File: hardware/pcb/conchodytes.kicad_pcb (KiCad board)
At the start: 4 copper layers, 39 x 81.5 mm, 62 parts, among them J1 Conn_02x03_Odd_Even, J10 Battery, J48 USB_C_Receptacle_USB2.0_16P, Q2 AO3407, Q4 FS8205, SW1 Left click, SW2 Right Click, SW3 Middle click, SW54 SW_SPDT, U100 LDO 1V8, U18 TP4056-42-ESOP8, U2 PMW3360, U20 HT7833, U23 DW01A, U54 USBLC6-2SC6, U6 ESP32-S3-WROOM-1, U8 NRF24L01_Breakout

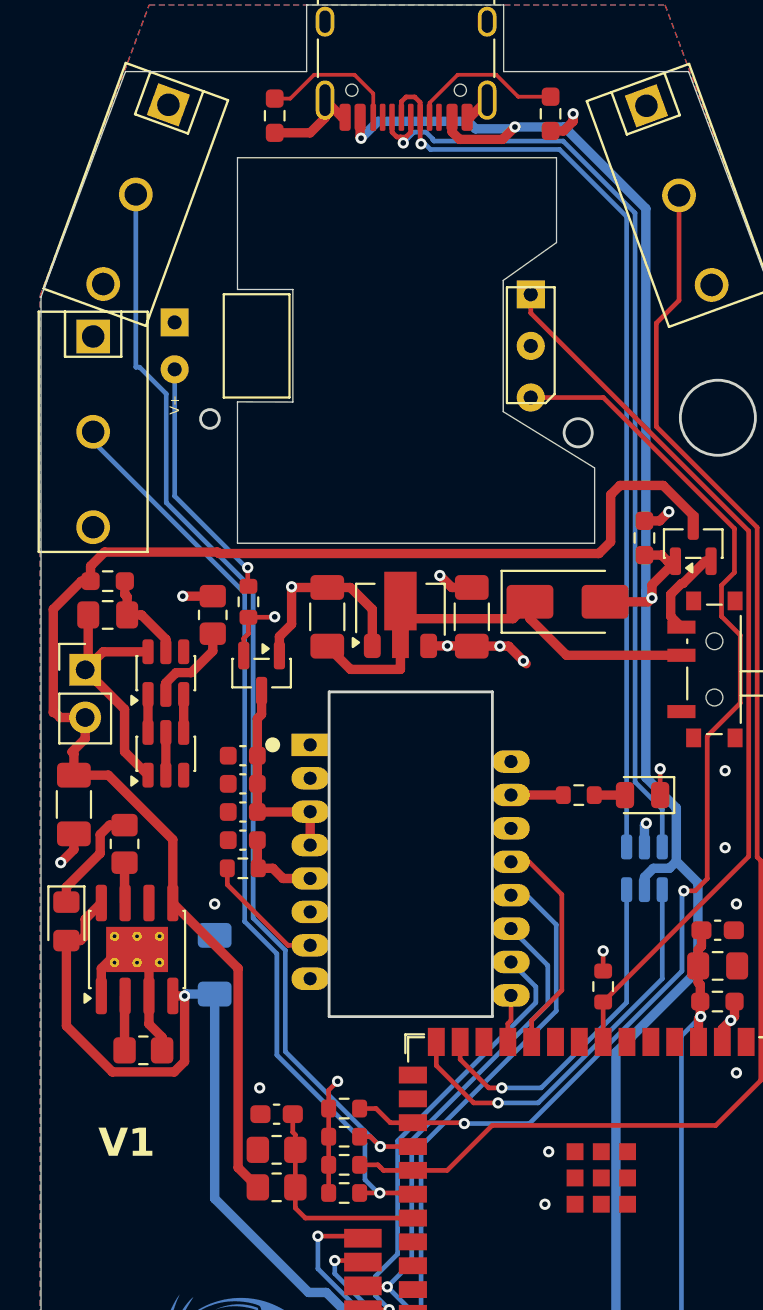
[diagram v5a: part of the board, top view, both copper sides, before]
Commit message: sérigraphie, logos annotés, prêt pour la pré-release
Mae a posé « Conchodytes » et « V1.0.0 08/2026 By mornepousse » au dos, plus le
logo Niphargus en cuivre et le symbole Open Source Hardware.

Les deux logos portaient la référence REF** : annotés HS1 et HS2, sinon le
prochain F8 les traiterait comme des composants fantômes.

Baseline re-référencée sur cet état (DRC 26/20, ERC 14/14) : la sérigraphie
ajoute 1 warning text_thickness, assumé.

Co-Authored-By: Claude Opus 5 <noreply@anthropic.com>
Claude-Session: https://claude.ai/code/session_01GfX5RmekmQi78Dm37qsT4Z
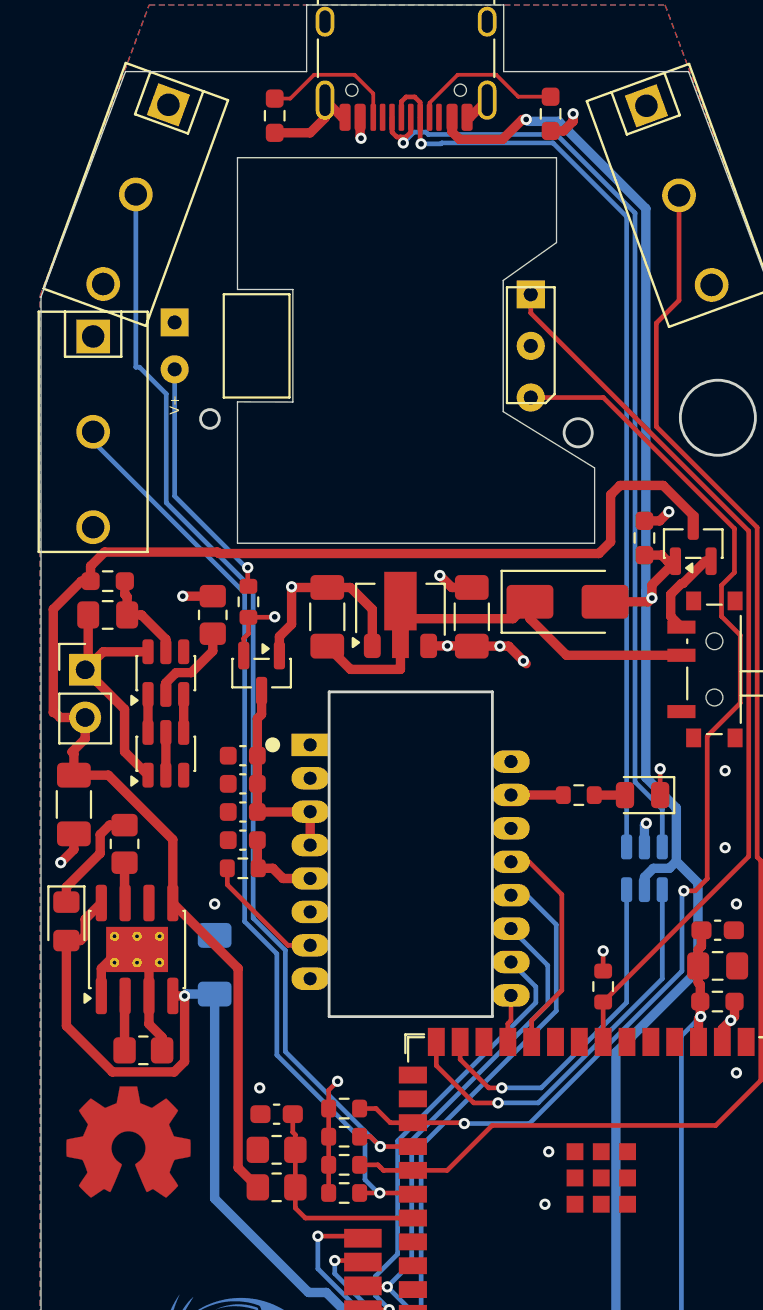
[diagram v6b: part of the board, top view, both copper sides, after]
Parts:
- added HS2: OSHW-Symbol_6.7x6mm_Copper, Symbol:OSHW-Symbol_6.7x6mm_Copper, F.Cu at (81.5, 131.9)
- renumbered REF** to HS1
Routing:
- net +5V: track 166.5 -> 167.7 mm
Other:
- board text added: "V1.0.0 08/2026 By mornepousse"
- board text removed: "V1"

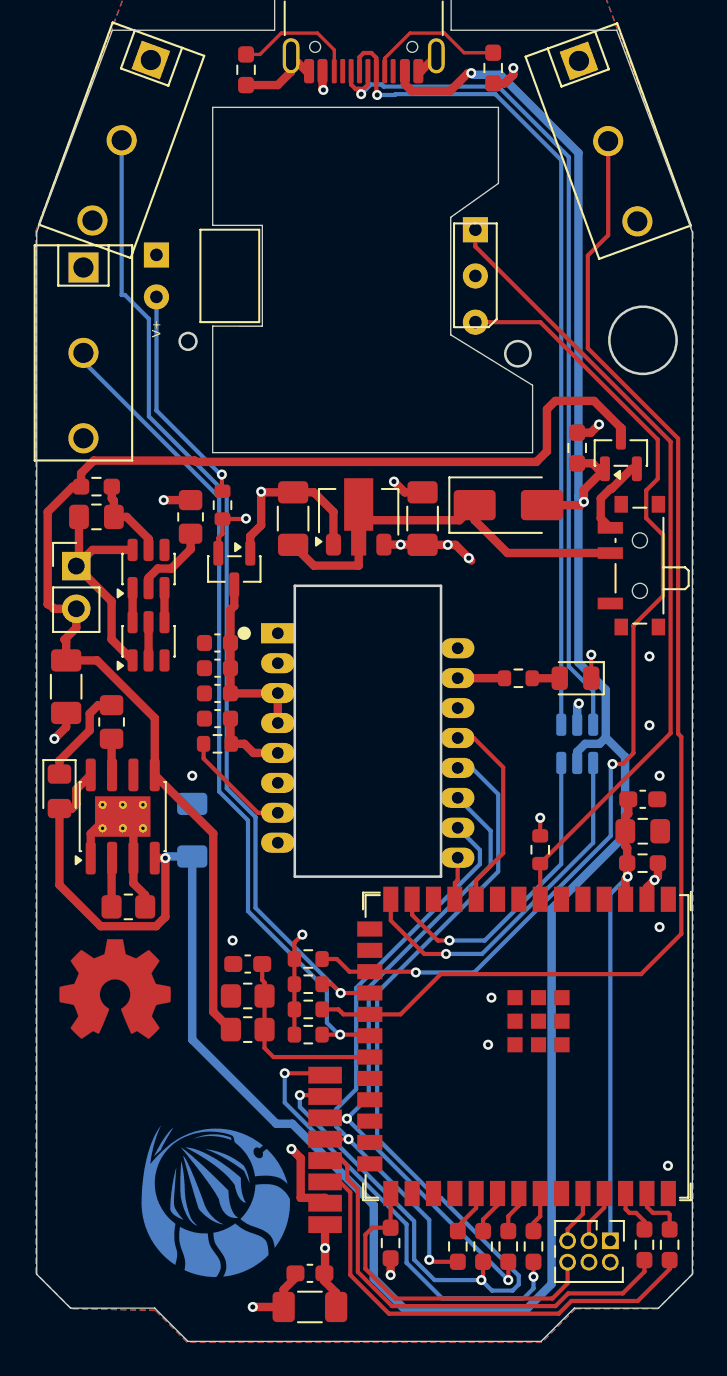
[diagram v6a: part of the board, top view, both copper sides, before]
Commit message: contacts NC des trois clics : anti-rebond par SPDT
Les switches de la coque M100 sont des SPDT. Le schema n'exploitait que COM et
NO, les pins NC portaient un no_connect et leurs pads restaient en l'air.

On lit maintenant les DEUX contacts. Au repos NC est ferme sur COM donc bas et
NO ouvert donc haut ; au clic ils s'inversent. Pendant le rebond les deux sont
hauts : le firmware garde alors l'etat precedent, ce qui supprime le double-clic
sans aucun filtrage temporel.

  SW_LEFT_NC  -> GPIO4    SW_RIGHT_NC -> GPIO5    SW_MID_NC -> GPIO6
  pull-ups 10 k R108/R109/R110, en miroir des R105-R107 des NO

L'ERC y GAGNE 3 erreurs (14 -> 11) : GPIO4/5/6 etaient des pins libres
signalees pin_not_connected. Netlist verifiee, chaque net NC a exactement
3 noeuds. DRC 26/20 inchange, 0 pad non connecte. Placement et routage par Mae.

CORRECTION DE DOCUMENTATION : le README donnait "SW_LEFT 18, SW_RIGHT 19,
SW_MID 20" — ce sont les NUMEROS DE BROCHE du module, pas les GPIO, qui valent
10/11/12. Idem SNS_NCS (GPIO17, broche 10) et SNS_MOTION (GPIO18, broche 11).
Verifie en recoupant lib_symbols, les fils et la netlist. Le tableau donne
desormais les deux colonnes. Le module au BOM est un N8R2 (C2913204), pas le
N16R8 dont parlait le README — la mention de PSRAM octale est retiree.

Co-Authored-By: Claude Opus 5 <noreply@anthropic.com>
Claude-Session: https://claude.ai/code/session_01GfX5RmekmQi78Dm37qsT4Z
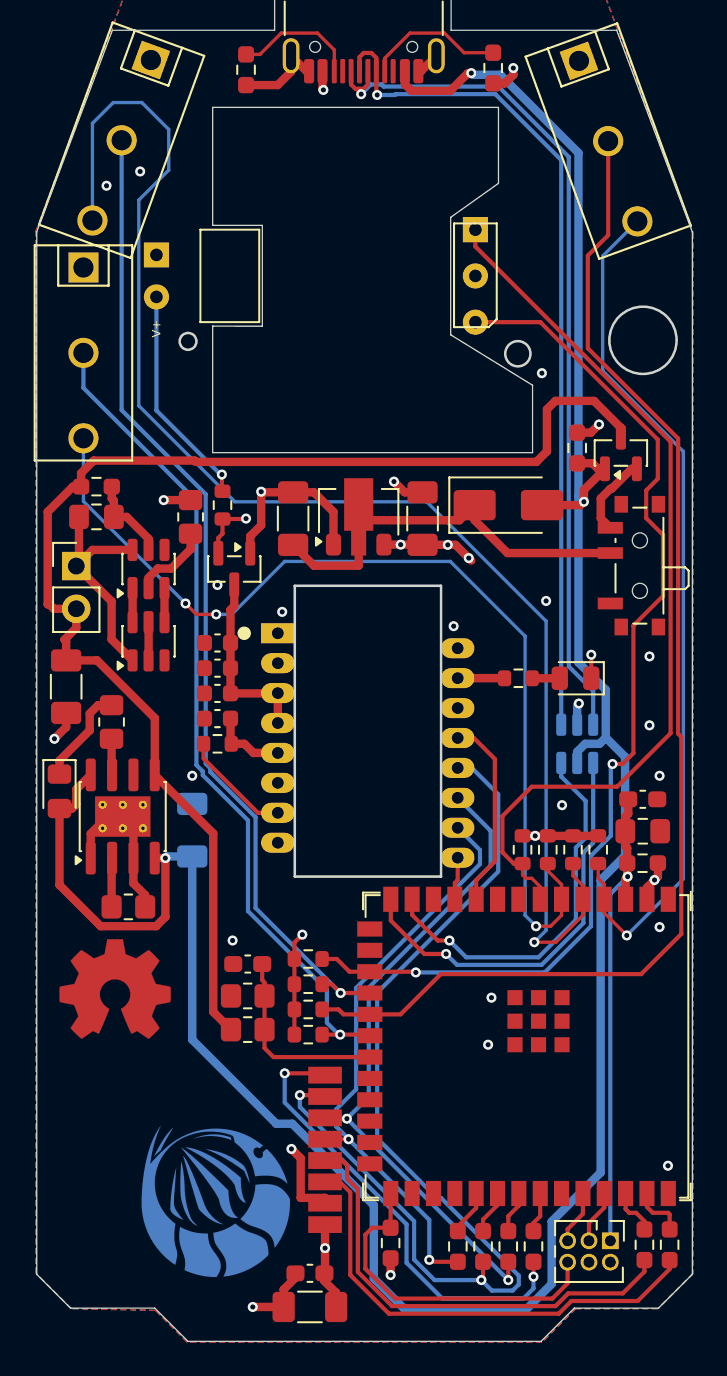
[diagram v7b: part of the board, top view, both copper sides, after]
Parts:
- added R108: 10k, Resistor_SMD:R_0603_1608Metric, F.Cu at (108.8, 123.6)
- added R109: 10k, Resistor_SMD:R_0603_1608Metric, F.Cu at (110.2, 123.6)
- added R110: 10k, Resistor_SMD:R_0603_1608Metric, F.Cu at (107.2, 123.6)
- moved R103 1.05 mm to (105.8, 123.6)
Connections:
- SW1 pad 3: unconnected-(SW1-NC-Pad3) -> SW_LEFT_NC
- SW2 pad 3: unconnected-(SW2-NC-Pad3) -> SW_RIGHT_NC
- SW3 pad 3: unconnected-(SW3-NC-Pad3) -> SW_MID_NC
- U6 pad 4: unconnected-(U6-GPIO4/TOUCH4/ADC1_CH3-Pad4) -> SW_RIGHT_NC
- U6 pad 5: unconnected-(U6-GPIO5/TOUCH5/ADC1_CH4-Pad5) -> SW_LEFT_NC
- U6 pad 6: unconnected-(U6-GPIO6/TOUCH6/ADC1_CH5-Pad6) -> SW_MID_NC
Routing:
- net SW_LEFT_NC: track 0.00 -> 84.5 mm, vias 0 -> 1
- net SW_MID_NC: track 0.00 -> 58.9 mm, vias 0 -> 3
- net SW_RIGHT_NC: track 0.00 -> 51.7 mm, vias 0 -> 1
- net ENC_A: track 47.9 -> 53.2 mm
- net D-_s3: track 18.3 -> 22.8 mm
- net +3.3V: track 31.1 -> 34.5 mm
- net D+_s3: track 21.6 -> 24.6 mm
- net ENC_B: track 60.5 -> 63.0 mm
- net GND: vias 18 -> 26

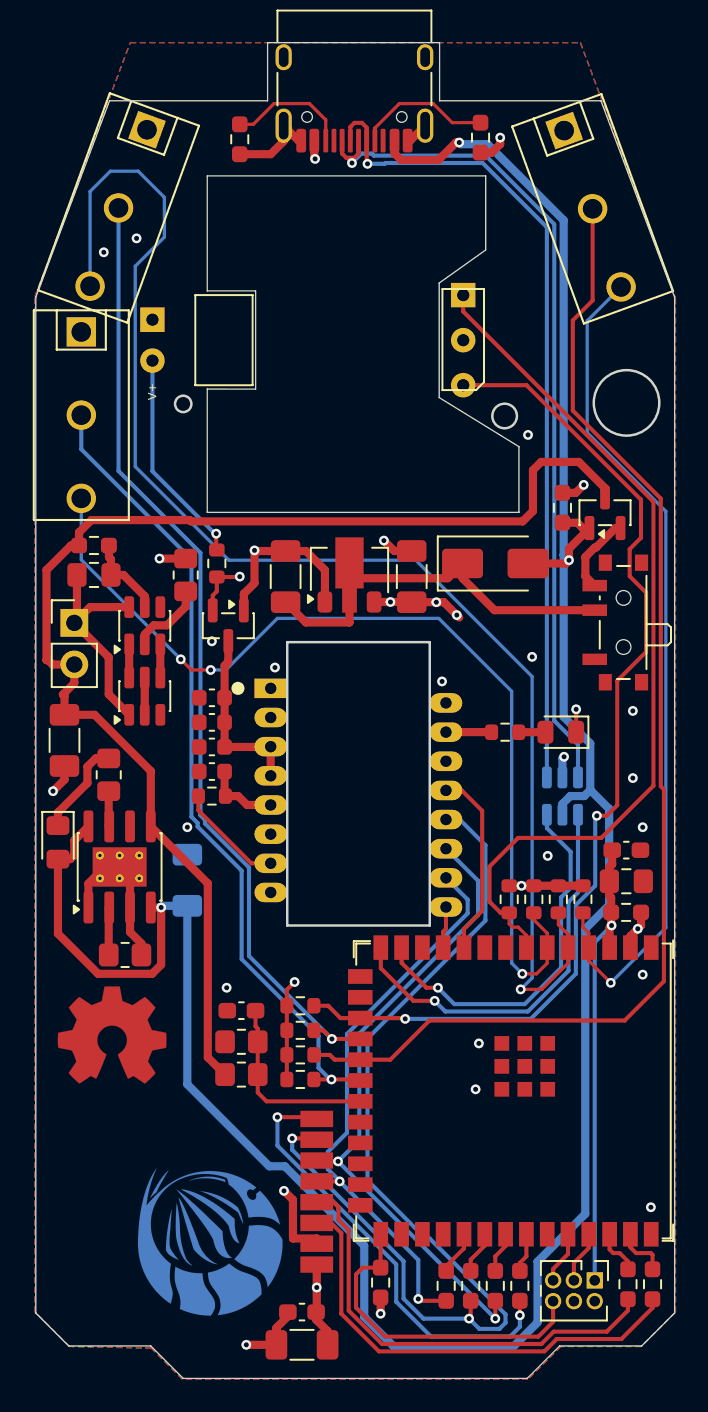
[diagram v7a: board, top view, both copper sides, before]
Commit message: schema REV2 : LQ1 recable, D100 supprimee, VBAT_SENSE sur ADC1, U100 corrige
LQ1 etait cable a l'envers depuis le portage du fork USB-Mouse. Le symbole
Optical_Mouse:LQ ne nommait ses broches que "1, 2, 3", sans fonction, et le
portage a suppose un double phototransistor A/COM/B. Le schema d'origine de la
M100 dit autre chose : broche 1 = DATA, 2 = VCC, 3 = GND.

La carte alimentait donc le capteur a l'envers — son VCC a la masse, sa masse
tiree au 3,3 V par R104. Le courant passait par la diode de substrat interne et
clampait les deux nets a 0,65 V, insensible a la lumiere comme au pilotage.
Deux LQ1 ont ete dessoudes avant que la confrontation au schema source ne donne
la reponse.

  - LQ1.2 -> +3V3, LQ1.3 -> GND, LQ1.1 (DATA) reste sur ENC_A / GPIO7
  - LD1 cathode -> R102 -> GPIO9, renomme ENC_LED : la LED de molette devient
    pilotable, comme sur la M100 d'origine. Gain d'autonomie, et un diagnostic
    qui aurait pris une minute au lieu d'une journee.
  - R102 = 820 ohms : 2,6 mA, le point de fonctionnement d'origine transpose
    du 5 V USB au 3,3 V
  - R104 = 0 ohm (pont vers la masse), R103 conservee
  - symbole LQ : broches nommees DATA / VCC / GND, dans le cache et dans
    optical_mouse.lib, pour que l'erreur soit impossible a refaire

D100 supprimee : le PMW3389 embarque sa LED IR (broche 15 LED_P = anode). La
LED externe etait de surcroit montee a l'envers et bloquait le courant, rendant
le capteur aveugle. R101 = 16 ohms alimentee depuis le rail capteur, renomme
+1V8 -> +2V0.

VBAT_SENSE passe de U6.21 (GPIO13, ADC2_CH2) a U6.12 (GPIO8, ADC1_CH7) :
l'ADC2 de l'ESP32-S3 est partage avec le driver WiFi.

U100 : les numeros de pad du symbole sont corriges — VI porte le pad 3 et VO le
pad 2, soit le brochage reel du XC6206 en SOT-23. Le schema cesse de mentir et
la netlist devient juste d'elle-meme.

Co-Authored-By: Claude Opus 5 (1M context) <noreply@anthropic.com>
Claude-Session: https://claude.ai/code/session_01VhxWZJVUd4SHAcp3eUFVJV
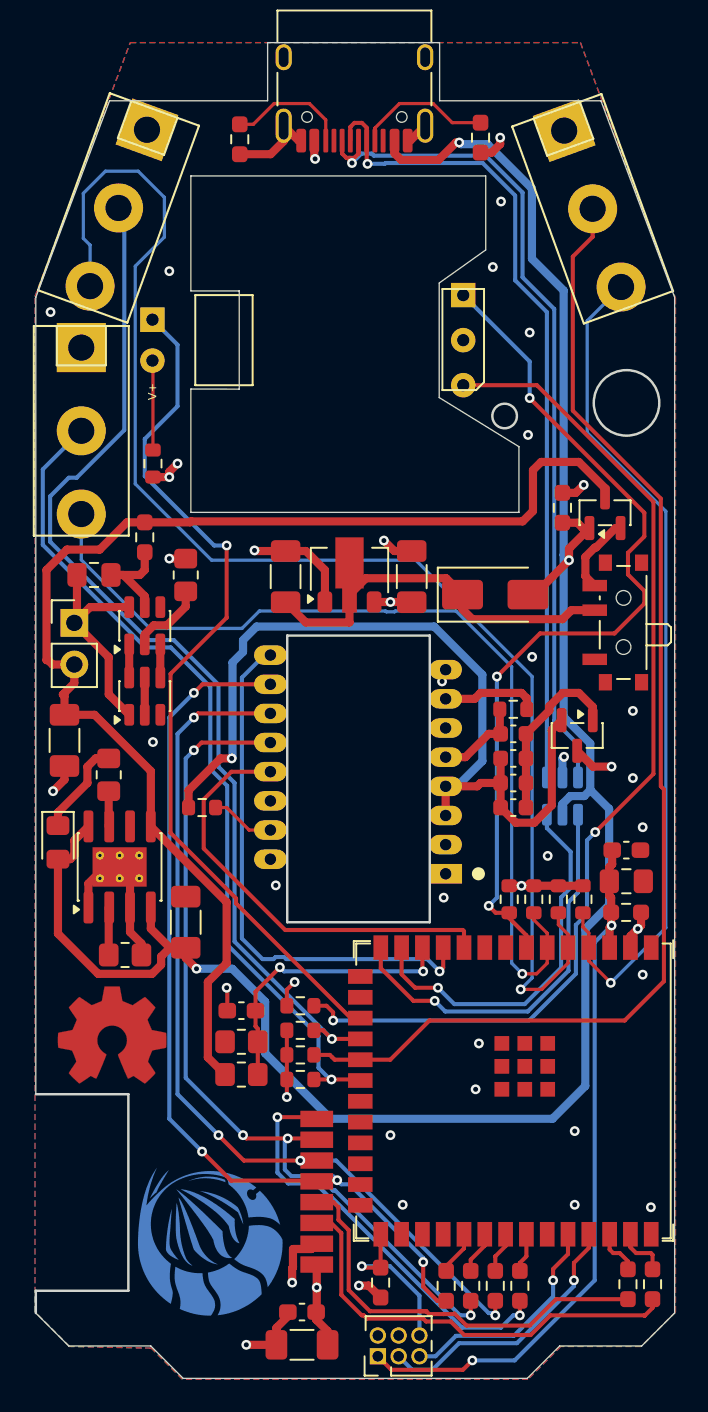
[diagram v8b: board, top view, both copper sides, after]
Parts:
- removed D100: IR 940nm, LED_SMD:LED_0805_2012Metric
- C20: moved to F.Cu
- R101: value 100 -> 16
- R102: value 270 -> 820
- R104: value 10k -> 0
- U100: value LDO 1V8 -> LDO 2V0
- U2: value PMW3360 -> PMW3389
- moved U100 22.3 mm to (109.9, 113.6)
- moved C103 19.6 mm to (106.0, 118.0), turned to 0 degrees
- moved R100 19.1 mm to (106.0, 112.0), turned to 0 degrees
- moved R101 19.1 mm to (87.0, 118.0), turned to 180 degrees
- moved C101 18.8 mm to (106.0, 116.5), turned to 0 degrees
- moved C102 18.5 mm to (106.0, 113.5), turned to 0 degrees
- moved C100 18.4 mm to (106.0, 115.0), turned to 0 degrees
- moved J1 14.0 mm to (97.7, 151.5), turned to 90 degrees
- moved R102 7.24 mm to (84.0, 97.0)
- moved R70 3.14 mm to (83.5, 101.5), turned to -90 degrees
- moved C20 2.56 mm to (86.0, 125.0)
- moved D52 1.90 mm to (104.9, 105.0)
- moved SW3 0.96 mm to (79.6, 95.0)
- turned U2 to 180 degrees
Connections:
- C100 pad 1: +1V8 -> +2V0
- C101 pad 1: +1V8 -> +2V0
- C103 pad 1: +1V8 -> +2V0
- LD1 pad 1: GND -> ENC_LED
- LQ1 pad 2: GND -> +3.3V
- LQ1 pad 3: ENC_B -> Net-(LQ1-Pad3)
- R101 pad 2: Net-(D100-A) -> +2V0
- R104 pad 1: ENC_B -> Net-(LQ1-Pad3)
- R104 pad 2: +3.3V -> GND
- U100 pad 2: +3.3V -> +2V0
- U100 pad 3: +1V8 -> +3.3V
- U2 pad 3: +1V8 -> +2V0
- U2 pad 4: +1V8 -> +2V0
- U6 pad 12: unconnected-(U6-GPIO8/TOUCH8/ADC1_CH7/SUBSPICS1-Pad12) -> VBAT_SENSE
- U6 pad 17: ENC_B -> ENC_LED
- U6 pad 21: VBAT_SENSE -> unconnected-(U6-GPIO13/TOUCH13/ADC2_CH2/FSPIQ/FSPIIO7/SUBSPIQ-Pad21)
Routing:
- net Net-(LQ1-Pad3): track 0.00 -> 63.2 mm, vias 0 -> 2
- net ENC_B: track 63.0 -> 0.00 mm, vias 2 -> 0
- net +2V0: track 0.00 -> 53.9 mm, vias 0 -> 1
- net ENC_LED: track 0.00 -> 53.2 mm, vias 0 -> 1
- net SNS_MOTION: track 2.55 -> 32.8 mm, vias 0 -> 1
- net +5V: track 167.7 -> 142.0 mm
- net SCK_L: track 35.3 -> 54.4 mm, vias 2 -> 4
- net /mcu/EN: track 28.1 -> 43.9 mm, vias 1 -> 2
- net MOSI_L: track 39.4 -> 55.1 mm, vias 2 -> 4
- net SNS_NCS: track 11.5 -> 26.8 mm
- net /mcu/TX: track 3.19 -> 16.7 mm, vias 0 -> 1
- net +1V8: track 11.2 -> 0.00 mm
- net /mcu/RX: track 3.19 -> 13.9 mm, vias 0 -> 1
- net /mcu/IO0: track 20.1 -> 9.93 mm, vias 0 -> 1
- net MISO_L: track 61.2 -> 52.6 mm, vias 2 -> 4
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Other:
- outline, holes or cut-outs redrawn
- board text added: "REV2.0.0 08/2026 By mornepousse"
- board text removed: "V1.0.0 08/2026 By mornepousse"
